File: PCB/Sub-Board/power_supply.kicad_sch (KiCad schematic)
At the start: 7 parts, among them U1 TPS629210DRLR

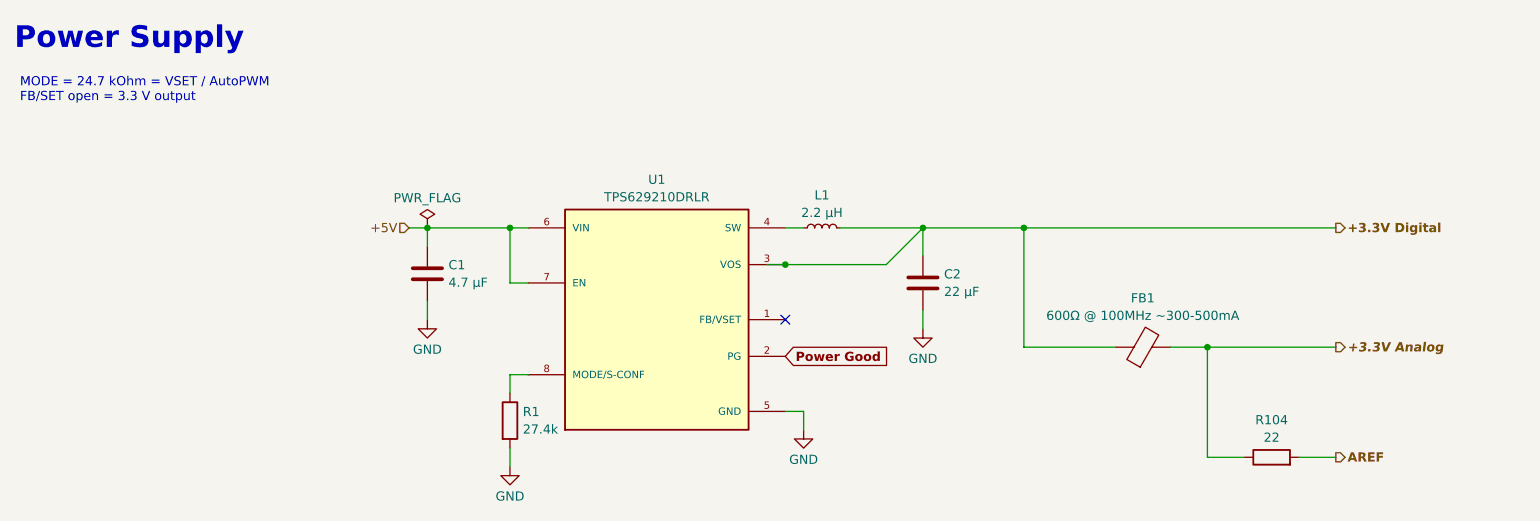
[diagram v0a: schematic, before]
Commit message: Sub-Board PCB before ERC
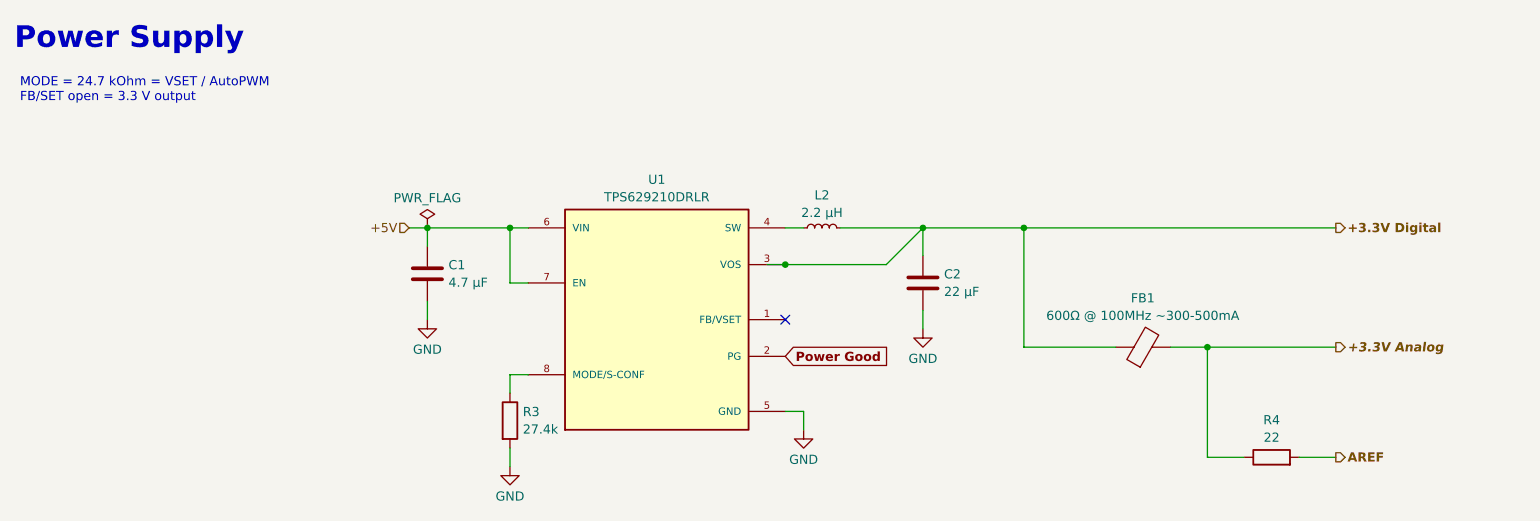
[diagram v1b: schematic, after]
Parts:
- renumbered L1 to L2, R1 to R3, R104 to R4
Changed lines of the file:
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@@
 		(dnp no)
 		(fields_autoplaced yes)
-		(property "Reference" "#PWR07"
+		(property "Reference" "#PWR05"
 			(at 93.98 92.71 0)
 			(effects
@@
 			(project "Template"
 				(path "/f9cf8dcb-b299-4fad-bb24-e1dfd3a00b1a/67d6849d-c619-4fbf-9b28-62bd1b7fad7b"
-					(reference "#PWR07")
+					(reference "#PWR05")
 					(unit 1)
 				)
@@
 		(dnp no)
 		(fields_autoplaced yes)
-		(property "Reference" "#PWR03"
+		(property "Reference" "#PWR04"
 			(at 82.55 72.39 0)
 			(effects
@@
 			(project "Template"
 				(path "/f9cf8dcb-b299-4fad-bb24-e1dfd3a00b1a/67d6849d-c619-4fbf-9b28-62bd1b7fad7b"
-					(reference "#PWR03")
+					(reference "#PWR04")
 					(unit 1)
 				)
@@
 		(dnp no)
 		(fields_autoplaced yes)
-		(property "Reference" "#PWR04"
+		(property "Reference" "#PWR07"
 			(at 151.13 73.66 0)
 			(effects
@@
 			(project "Template"
 				(path "/f9cf8dcb-b299-4fad-bb24-e1dfd3a00b1a/67d6849d-c619-4fbf-9b28-62bd1b7fad7b"
-					(reference "#PWR04")
+					(reference "#PWR07")
 					(unit 1)
 				)
@@
 		(dnp no)
 		(fields_autoplaced yes)
-		(property "Reference" "L1"
+		(property "Reference" "L2"
 			(at 137.16 48.8167 90)
 			(effects
@@
 			(project "Template"
 				(path "/f9cf8dcb-b299-4fad-bb24-e1dfd3a00b1a/67d6849d-c619-4fbf-9b28-62bd1b7fad7b"
-					(reference "L1")
+					(reference "L2")
 					(unit 1)
 				)
@@
 		(dnp no)
 		(fields_autoplaced yes)
-		(property "Reference" "R104"
+		(property "Reference" "R4"
 			(at 199.39 79.9295 90)
 			(effects
@@
 			(project ""
 				(path "/f9cf8dcb-b299-4fad-bb24-e1dfd3a00b1a/67d6849d-c619-4fbf-9b28-62bd1b7fad7b"
-					(reference "R104")
+					(reference "R4")
 					(unit 1)
 				)
@@
 		(dnp no)
 		(fields_autoplaced yes)
-		(property "Reference" "R1"
+		(property "Reference" "R3"
 			(at 95.758 78.7978 0)
 			(effects
@@
 			(project "Template"
 				(path "/f9cf8dcb-b299-4fad-bb24-e1dfd3a00b1a/67d6849d-c619-4fbf-9b28-62bd1b7fad7b"
-					(reference "R1")
-					(unit 1)
-				)
+					(reference "R3")
+					(unit 1)
+				)

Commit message: Sub-Board PCB after ERC
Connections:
- net Power Good: no longer names the net of U1.2 (PG)
- no-connect marks 1 -> 2
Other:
- moved on the sheet: R4
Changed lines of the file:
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@@
 	)
 	(junction
-		(at 132.08 58.42)
-		(diameter 0)
-		(color 0 0 0 0)
-	)
-	(junction
-		(at 190.5 69.85)
+		(at 203.2 69.85)
 		(diameter 0)
 		(color 0 0 0 0)
@@
 		(at 132.08 66.04)
 	)
-	(wire
-		(pts
-			(xy 129.54 58.42) (xy 132.08 58.42)
-		)
-		(stroke
-			(width 0)
-			(type default)
-		)
+	(no_connect
+		(at 132.08 71.12)
 	)
 	(wire
@@
 	(wire
 		(pts
-			(xy 190.5 85.09) (xy 190.5 69.85)
-		)
-		(stroke
-			(width 0)
-			(type default)
-		)
-	)
-	(wire
-		(pts
 			(xy 132.08 53.34) (xy 134.62 53.34)
 		)
@@
 	(wire
 		(pts
-			(xy 190.5 69.85) (xy 208.28 69.85)
-		)
-		(stroke
-			(width 0)
-			(type default)
-		)
-	)
-	(wire
-		(pts
 			(xy 134.62 78.74) (xy 134.62 81.28)
 		)
@@
 	(wire
 		(pts
-			(xy 165.1 53.34) (xy 208.28 53.34)
+			(xy 165.1 53.34) (xy 215.9 53.34)
 		)
 		(stroke
@@
 	(wire
 		(pts
+			(xy 203.2 85.09) (xy 205.74 85.09)
+		)
+		(stroke
+			(width 0)
+			(type default)
+		)
+	)
+	(wire
+		(pts
+			(xy 203.2 69.85) (xy 215.9 69.85)
+		)
+		(stroke
+			(width 0)
+			(type default)
+		)
+	)
+	(wire
+		(pts
 			(xy 165.1 69.85) (xy 177.8 69.85)
 		)
@@
 	(wire
 		(pts
+			(xy 203.2 69.85) (xy 203.2 85.09)
+		)
+		(stroke
+			(width 0)
+			(type default)
+		)
+	)
+	(wire
+		(pts
 			(xy 82.55 63.5) (xy 82.55 66.04)
 		)
@@
 	(wire
 		(pts
-			(xy 195.58 85.09) (xy 190.5 85.09)
-		)
-		(stroke
-			(width 0)
-			(type default)
-		)
-	)
-	(wire
-		(pts
 			(xy 165.1 53.34) (xy 165.1 69.85)
 		)
@@
 	(wire
 		(pts
-			(xy 185.42 69.85) (xy 190.5 69.85)
-		)
-		(stroke
-			(width 0)
-			(type default)
-		)
-	)
-	(wire
-		(pts
-			(xy 203.2 85.09) (xy 208.28 85.09)
-		)
-		(stroke
-			(width 0)
-			(type default)
-		)
-	)
-	(global_label "Power Good"
-		(shape input)
-		(at 132.08 71.12 0)
-		(fields_autoplaced yes)
-		(effects
-			(font
-				(size 1.27 1.27)
-				(thickness 0.254)
-				(bold yes)
-			)
-			(justify left)
-		)
-		(property "Intersheetrefs" "${INTERSHEET_REFS}"
-			(at 146.8501 71.12 0)
-			(effects
-				(font
-					(size 1.27 1.27)
-				)
-				(justify left)
-				(hide yes)
-			)
+			(xy 185.42 69.85) (xy 203.2 69.85)
+		)
+		(stroke
+			(width 0)
+			(type default)
+		)
+	)
+	(wire
+		(pts
+			(xy 213.36 85.09) (xy 215.9 85.09)
+		)
+		(stroke
+			(width 0)
+			(type default)
 		)
 	)
@@
 	(hierarchical_label "+3.3V Digital"
 		(shape output)
-		(at 208.28 53.34 0)
+		(at 215.9 53.34 0)
 		(effects
 			(font
@@
 	(hierarchical_label "AREF"
 		(shape output)
-		(at 208.28 85.09 0)
+		(at 215.9 85.09 0)
 		(effects
 			(font
@@
 	(hierarchical_label "+3.3V Analog"
 		(shape output)
-		(at 208.28 69.85 0)
+		(at 215.9 69.85 0)
 		(effects
 			(font
@@
 	(symbol
 		(lib_id "power:PWR_FLAG")
-		(at 82.55 53.34 0)
+		(at 165.1 53.34 0)
 		(unit 1)
 		(exclude_from_sim no)
@@
 		(dnp no)
 		(fields_autoplaced yes)
-		(property "Reference" "#FLG01"
-			(at 82.55 51.435 0)
+		(property "Reference" "#FLG04"
+			(at 165.1 51.435 0)
 			(effects
 				(font
@@
 		)
 		(property "Value" "PWR_FLAG"
-			(at 82.55 49.2069 0)
+			(at 165.1 49.2069 0)
 			(effects
 				(font
@@
 		)
 		(property "Footprint" ""
-			(at 82.55 53.34 0)
+			(at 165.1 53.34 0)
 			(effects
 				(font
@@
 		)
 		(property "Datasheet" "~"
-			(at 82.55 53.34 0)
+			(at 165.1 53.34 0)
 			(effects
 				(font
@@
 		)
 		(property "Description" "Special symbol for telling ERC where power comes from"
-			(at 82.55 53.34 0)
+			(at 165.1 53.34 0)
 			(effects
 				(font
@@
 		)
 		(instances
-			(project "Template"
+			(project ""
 				(path "/f9cf8dcb-b299-4fad-bb24-e1dfd3a00b1a/67d6849d-c619-4fbf-9b28-62bd1b7fad7b"
-					(reference "#FLG01")
+					(reference "#FLG04")
+					(unit 1)
+				)
+			)
+		)
+	)
+	(symbol
+		(lib_id "power:PWR_FLAG")
+		(at 203.2 69.85 0)
+		(unit 1)
+		(exclude_from_sim no)
+		(in_bom yes)
+		(on_board yes)
+		(dnp no)
+		(fields_autoplaced yes)
+		(property "Reference" "#FLG05"
+			(at 203.2 67.945 0)
+			(effects
+				(font
+					(size 1.27 1.27)
+				)
+				(hide yes)
+			)
+		)
+		(property "Value" "PWR_FLAG"
+			(at 203.2 65.7169 0)
+			(effects
+				(font
+					(size 1.27 1.27)
+				)
+			)
+		)
+		(property "Footprint" ""
+			(at 203.2 69.85 0)
+			(effects
+				(font
+					(size 1.27 1.27)
+				)
+				(hide yes)
+			)
+		)
+		(property "Datasheet" "~"
+			(at 203.2 69.85 0)
+			(effects
+				(font
+					(size 1.27 1.27)
+				)
+				(hide yes)
+			)
+		)
+		(property "Description" "Special symbol for telling ERC where power comes from"
+			(at 203.2 69.85 0)
+			(effects
+				(font
+					(size 1.27 1.27)
+				)
+				(hide yes)
+			)
+		)
+		(pin "1"
+		)
+		(instances
+			(project "Sub-Board"
+				(path "/f9cf8dcb-b299-4fad-bb24-e1dfd3a00b1a/67d6849d-c619-4fbf-9b28-62bd1b7fad7b"
+					(reference "#FLG05")
 					(unit 1)
 				)
@@
 	(symbol
 		(lib_id "Device:R")
-		(at 199.39 85.09 90)
+		(at 209.55 85.09 90)
 		(unit 1)
 		(exclude_from_sim no)
@@
 		(fields_autoplaced yes)
 		(property "Reference" "R4"
-			(at 199.39 79.9295 90)
+			(at 209.55 79.9295 90)
 			(effects
 				(font
@@
 		)
 		(property "Value" "22"
-			(at 199.39 82.3538 90)
+			(at 209.55 82.3538 90)
 			(effects
 				(font
@@
 		)
 		(property "Footprint" ""
-			(at 199.39 86.868 90)
+			(at 209.55 86.868 90)
 			(effects
 				(font
@@
 		)
 		(property "Datasheet" "~"
-			(at 199.39 85.09 0)
+			(at 209.55 85.09 0)
 			(effects
 				(font
@@
 		)
 		(property "Description" "Resistor"
-			(at 199.39 85.09 0)
-			(effects
-				(font
+			(at 209.55 85.09 0)
+			(effects
+				(font

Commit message: Sub-Board PCB: Footprint assignments
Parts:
- C1: footprint (none) -> Capacitor_SMD:C_0805_2012Metric
- C2: footprint (none) -> Capacitor_SMD:C_1206_3216Metric
- FB1: footprint (none) -> Inductor_SMD:L_0603_1608Metric
- L2: footprint (none) -> Inductor_SMD:L_0805_2012Metric
- R3, R4: footprint (none) -> Resistor_SMD:R_0603_1608Metric
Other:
- title: Modular Music Controller – Power Supply -> Modular Music Controller / Sub-Board / Power Supply
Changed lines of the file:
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@@
 	(paper "A4")
 	(title_block
-		(title "Modular Music Controller – Power Supply")
+		(title "Modular Music Controller / Sub-Board / Power Supply")
 		(date "2025-11-02")
 		(rev "1")
@@
 			)
 		)
-		(property "Footprint" ""
+		(property "Footprint" "Inductor_SMD:L_0603_1608Metric"
 			(at 181.61 71.628 90)
 			(effects
@@
 			)
 		)
-		(property "Footprint" ""
+		(property "Footprint" "Capacitor_SMD:C_1206_3216Metric"
 			(at 152.0952 64.77 0)
 			(effects
@@
 			)
 		)
-		(property "Footprint" ""
+		(property "Footprint" "Capacitor_SMD:C_0805_2012Metric"
 			(at 83.5152 63.5 0)
 			(effects
@@
 			)
 		)
-		(property "Footprint" ""
+		(property "Footprint" "Inductor_SMD:L_0805_2012Metric"
 			(at 137.16 53.34 0)
 			(effects
@@
 			)
 		)
-		(property "Footprint" ""
+		(property "Footprint" "Resistor_SMD:R_0603_1608Metric"
 			(at 209.55 86.868 90)
 			(effects
@@
 			)
 		)
-		(property "Footprint" ""
+		(property "Footprint" "Resistor_SMD:R_0603_1608Metric"
 			(at 92.202 80.01 90)
 			(effects

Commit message: Sub Board PCB: PCB Layout (wip)
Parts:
- R3, R4: footprint Resistor_SMD:R_0603_1608Metric -> Resistor_SMD:R_0402_1005Metric
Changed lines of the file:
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@@
 			)
 		)
-		(property "Footprint" "Resistor_SMD:R_0603_1608Metric"
+		(property "Footprint" "Resistor_SMD:R_0402_1005Metric"
 			(at 209.55 86.868 90)
 			(effects
@@
 			)
 		)
-		(property "Footprint" "Resistor_SMD:R_0603_1608Metric"
+		(property "Footprint" "Resistor_SMD:R_0402_1005Metric"
 			(at 92.202 80.01 90)
 			(effects
